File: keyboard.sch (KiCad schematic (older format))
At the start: 81 parts, among them SW10 Z, SW11 3rd, SW12 F2, SW13 E, SW14 D, SW15 X, SW16 2nd, SW17 F3, SW18 R, SW19 F, SW2 lock, SW20 C, SW21 store, SW22 F4, SW23 T, SW24 G, SW25 V, SW26 F5, SW27 Y, SW28 H, SW29 B, SW3 F1, SW30 spc, SW31 U, SW32 J, SW33 N, SW34 F6, SW35 I, SW36 K, SW37 M, SW38 equal, SW39 F7, SW4 Q, SW40 O, SW41 L, SW42 zilde, SW43 left arrow, SW44 F8, SW45 P, SW46 enter, SW47 2nd_r, SW48 menu, SW49 clear, SW5 A, SW50 ln, SW51 sin, SW52 (, SW53 7, SW54 4, SW55 1, SW56 0, SW57 esc, SW58 apps, SW59 cos, SW6 CAPS, SW60 ), SW61 8, SW62 5, SW63 2, SW64 dot, SW65 up, SW66 left, SW67 down, SW68 enter_r, SW69 tan, SW70 ,, SW71 9, SW72 6, SW73 3, SW74 negative, SW75 right, SW76 ^, SW77 ÷, SW78 ×, SW79 -, SW8 W, SW80 +, SW81 enter, SW9 S, U8 MCP23017_SS

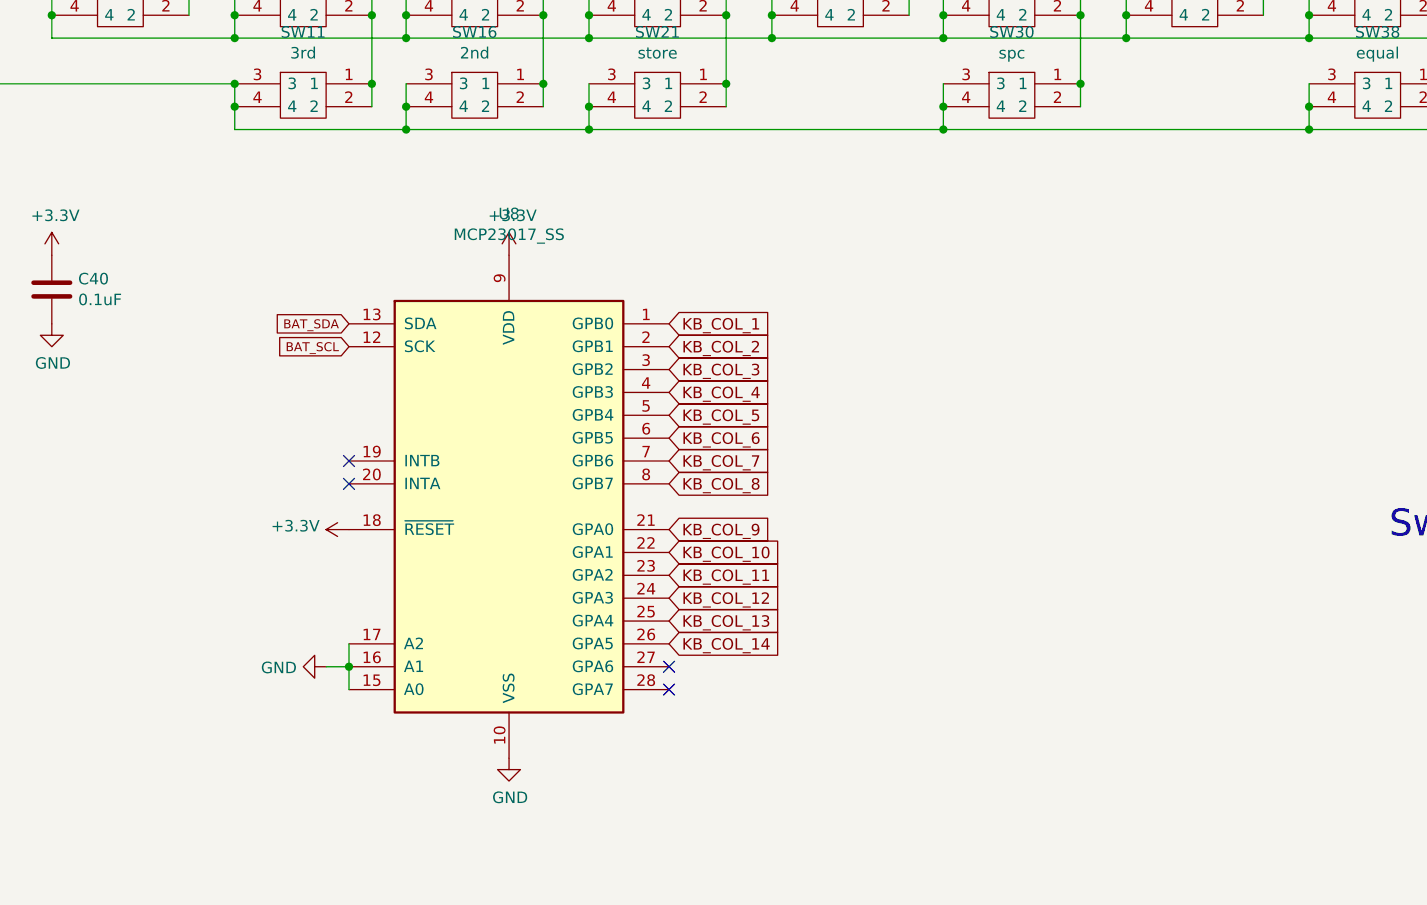
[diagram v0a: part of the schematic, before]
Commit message: Switch stuff around; Use two MCP
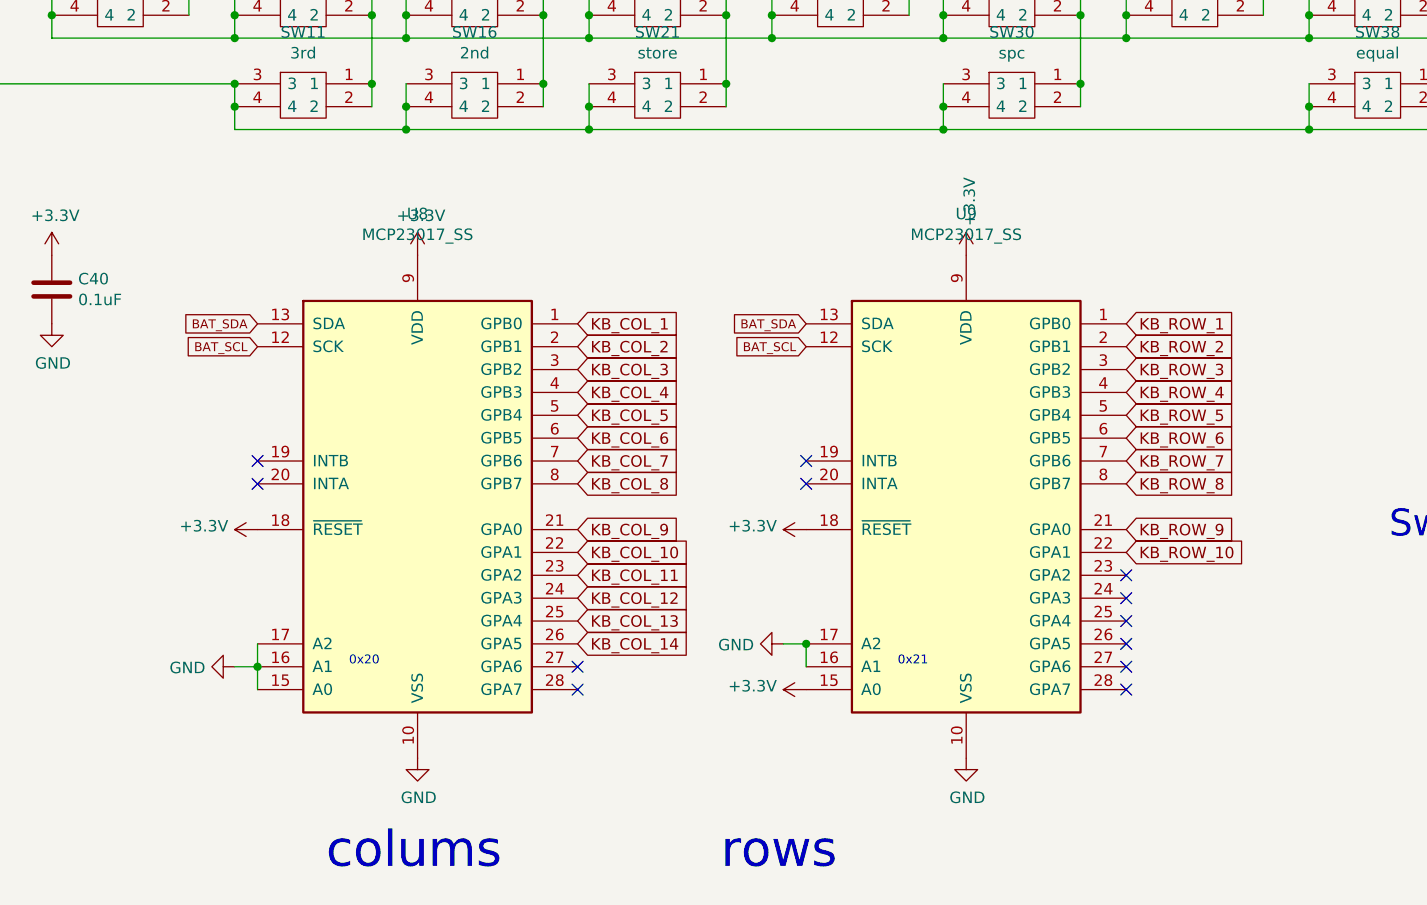
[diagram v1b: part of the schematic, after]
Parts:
- added U9: MCP23017_SS, Package_SO:SSOP-28_5.3x10.2mm_P0.65mm, symbol Interface_Expansion:MCP23017_SS
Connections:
- net +3V3: now also U9.15 (A0), U9.18 (~RESET~), U9.9 (VDD)
- net BAT_SCL: now also U9.12 (SCK)
- net BAT_SDA: now also U9.13 (SDA)
- net GND: now also U9.10 (VSS), U9.16 (A1), U9.17 (A2)
- net KB_ROW_1: now also U9.1 (GPB0)
- net KB_ROW_10: now also U9.22 (GPA1)
- net KB_ROW_2: now also U9.2 (GPB1)
- net KB_ROW_3: now also U9.3 (GPB2)
- net KB_ROW_4: now also U9.4 (GPB3)
- net KB_ROW_5: now also U9.5 (GPB4)
- net KB_ROW_6: now also U9.6 (GPB5)
- net KB_ROW_7: now also U9.7 (GPB6)
- net KB_ROW_8: now also U9.8 (GPB7)
- net KB_ROW_9: now also U9.21 (GPA0)
- no-connect marks 4 -> 12
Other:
- note added: "0x20"
- note added: "0x21"
- note added: "colums rows"
- moved on the sheet: U8
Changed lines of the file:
@@
 L Interface_Expansion:MCP23017_SS U8
 U 1 1 5F8EBE0E
-P 3200 6600
-F 0 "U8" H 3200 7881 50  0000 C CNN
-F 1 "MCP23017_SS" H 3200 7790 50  0000 C CNN
-F 2 "Package_SO:SSOP-28_5.3x10.2mm_P0.65mm" H 3400 5600 50  0001 L CNN
-F 3 "http://ww1.microchip.com/downloads/en/DeviceDoc/20001952C.pdf" H 3400 5500 50  0001 L CNN
-	1    3200 6600
-	1    0    0    -1
-$EndComp
-Text GLabel 3900 5800 2    50   Input ~ 0
+P 2800 6600
+F 0 "U8" H 2800 7881 50  0000 C CNN
+F 1 "MCP23017_SS" H 2800 7790 50  0000 C CNN
+F 2 "Package_SO:SSOP-28_5.3x10.2mm_P0.65mm" H 3000 5600 50  0001 L CNN
+F 3 "http://ww1.microchip.com/downloads/en/DeviceDoc/20001952C.pdf" H 3000 5500 50  0001 L CNN
+	1    2800 6600
+	1    0    0    -1
+$EndComp
+Text GLabel 3500 5800 2    50   Input ~ 0
 KB_COL_1
-Text GLabel 3900 5900 2    50   Input ~ 0
+Text GLabel 3500 5900 2    50   Input ~ 0
 KB_COL_2
-Text GLabel 3900 6000 2    50   Input ~ 0
+Text GLabel 3500 6000 2    50   Input ~ 0
 KB_COL_3
-Text GLabel 3900 6100 2    50   Input ~ 0
+Text GLabel 3500 6100 2    50   Input ~ 0
 KB_COL_4
-Text GLabel 3900 6200 2    50   Input ~ 0
+Text GLabel 3500 6200 2    50   Input ~ 0
 KB_COL_5
-Text GLabel 3900 6300 2    50   Input ~ 0
+Text GLabel 3500 6300 2    50   Input ~ 0
 KB_COL_6
-Text GLabel 3900 6400 2    50   Input ~ 0
+Text GLabel 3500 6400 2    50   Input ~ 0
 KB_COL_7
-Text GLabel 3900 6500 2    50   Input ~ 0
+Text GLabel 3500 6500 2    50   Input ~ 0
 KB_COL_8
-Text GLabel 3900 6700 2    50   Input ~ 0
+Text GLabel 3500 6700 2    50   Input ~ 0
 KB_COL_9
-Text GLabel 3900 6800 2    50   Input ~ 0
+Text GLabel 3500 6800 2    50   Input ~ 0
 KB_COL_10
-Text GLabel 3900 6900 2    50   Input ~ 0
+Text GLabel 3500 6900 2    50   Input ~ 0
 KB_COL_11
-Text GLabel 3900 7000 2    50   Input ~ 0
+Text GLabel 3500 7000 2    50   Input ~ 0
 KB_COL_12
-Text GLabel 3900 7100 2    50   Input ~ 0
+Text GLabel 3500 7100 2    50   Input ~ 0
 KB_COL_13
-Text GLabel 3900 7200 2    50   Input ~ 0
+Text GLabel 3500 7200 2    50   Input ~ 0
 KB_COL_14
-NoConn ~ 3900 7300
-NoConn ~ 3900 7400
-Text GLabel 2500 5800 0    39   Input ~ 0
+NoConn ~ 3500 7300
+NoConn ~ 3500 7400
+Text GLabel 2100 5800 0    39   Input ~ 0
 BAT_SDA
-Text GLabel 2500 5900 0    39   Input ~ 0
+Text GLabel 2100 5900 0    39   Input ~ 0
 BAT_SCL
 $Comp
 L power:GND #PWR0130
 U 1 1 5F97902E
-P 3200 7700
-F 0 "#PWR0130" H 3200 7450 50  0001 C CNN
-F 1 "GND" H 3205 7527 50  0000 C CNN
-F 2 "" H 3200 7700 50  0001 C CNN
-F 3 "" H 3200 7700 50  0001 C CNN
-	1    3200 7700
+P 2800 7700
+F 0 "#PWR0130" H 2800 7450 50  0001 C CNN
+F 1 "GND" H 2805 7527 50  0000 C CNN
+F 2 "" H 2800 7700 50  0001 C CNN
+F 3 "" H 2800 7700 50  0001 C CNN
+	1    2800 7700
 	1    0    0    -1
 $EndComp
@@
 L power:+3.3V #PWR0131
 U 1 1 5F9B509C
-P 3200 5500
-F 0 "#PWR0131" H 3200 5350 50  0001 C CNN
-F 1 "+3.3V" H 3215 5673 50  0000 C CNN
-F 2 "" H 3200 5500 50  0001 C CNN
-F 3 "" H 3200 5500 50  0001 C CNN
-	1    3200 5500
+P 2800 5500
+F 0 "#PWR0131" H 2800 5350 50  0001 C CNN
+F 1 "+3.3V" H 2815 5673 50  0000 C CNN
+F 2 "" H 2800 5500 50  0001 C CNN
+F 3 "" H 2800 5500 50  0001 C CNN
+	1    2800 5500
 	1    0    0    -1
 $EndComp
@@
 	1    0    0    -1
 $EndComp
-NoConn ~ 2500 6400
-NoConn ~ 2500 6500
+NoConn ~ 2100 6400
+NoConn ~ 2100 6500
 $Comp
 L power:+3.3V #PWR0134
 U 1 1 5F9F0EAC
-P 2500 6700
-F 0 "#PWR0134" H 2500 6550 50  0001 C CNN
-F 1 "+3.3V" V 2515 6828 50  0000 L CNN
-F 2 "" H 2500 6700 50  0001 C CNN
-F 3 "" H 2500 6700 50  0001 C CNN
-	1    2500 6700
+P 2100 6700
+F 0 "#PWR0134" H 2100 6550 50  0001 C CNN
+F 1 "+3.3V" V 2115 6828 50  0000 L CNN
+F 2 "" H 2100 6700 50  0001 C CNN
+F 3 "" H 2100 6700 50  0001 C CNN
+	1    2100 6700
 	0    -1   -1   0
 $EndComp
@@
 L power:GND #PWR0135
 U 1 1 5F9F243C
-P 2400 7300
-F 0 "#PWR0135" H 2400 7050 50  0001 C CNN
-F 1 "GND" V 2405 7172 50  0000 R CNN
-F 2 "" H 2400 7300 50  0001 C CNN
-F 3 "" H 2400 7300 50  0001 C CNN
-	1    2400 7300
+P 2000 7300
+F 0 "#PWR0135" H 2000 7050 50  0001 C CNN
+F 1 "GND" V 2005 7172 50  0000 R CNN
+F 2 "" H 2000 7300 50  0001 C CNN
+F 3 "" H 2000 7300 50  0001 C CNN
+	1    2000 7300
 	0    1    1    0
 $EndComp
 Wire Wire Line
-	2400 7300 2500 7300
-Wire Wire Line
-	2500 7200 2500 7300
-Connection ~ 2500 7300
-Wire Wire Line
-	2500 7300 2500 7400
+	2000 7300 2100 7300
+Wire Wire Line
+	2100 7200 2100 7300
+Connection ~ 2100 7300
+Wire Wire Line
+	2100 7300 2100 7400
 Text Notes 7050 6750 0    118  ~ 0
 Switches: FSM4JSMAATR
@@
 Wire Wire Line
 	10750 1650 10750 1750
+$Comp
+L Interface_Expansion:MCP23017_SS U9
+U 1 1 614CD4FF
+P 5200 6600
+F 0 "U9" H 5200 7881 50  0000 C CNN
+F 1 "MCP23017_SS" H 5200 7790 50  0000 C CNN
+F 2 "Package_SO:SSOP-28_5.3x10.2mm_P0.65mm" H 5400 5600 50  0001 L CNN
+F 3 "http://ww1.microchip.com/downloads/en/DeviceDoc/20001952C.pdf" H 5400 5500 50  0001 L CNN
+	1    5200 6600
+	1    0    0    -1
+$EndComp
+Text GLabel 4500 5800 0    39   Input ~ 0
+BAT_SDA
+Text GLabel 4500 5900 0    39   Input ~ 0
+BAT_SCL
+NoConn ~ 4500 6400
+NoConn ~ 4500 6500
+$Comp
+L power:+3.3V #PWR0125
+U 1 1 61601386
+P 4500 6700
+F 0 "#PWR0125" H 4500 6550 50  0001 C CNN
+F 1 "+3.3V" V 4515 6828 50  0000 L CNN
+F 2 "" H 4500 6700 50  0001 C CNN
+F 3 "" H 4500 6700 50  0001 C CNN
+	1    4500 6700
+	0    -1   -1   0
+$EndComp
+$Comp
+L power:GND #PWR0136
+U 1 1 61602403
+P 4400 7200
+F 0 "#PWR0136" H 4400 6950 50  0001 C CNN
+F 1 "GND" V 4405 7072 50  0000 R CNN
+F 2 "" H 4400 7200 50  0001 C CNN
+F 3 "" H 4400 7200 50  0001 C CNN
+	1    4400 7200
+	0    1    1    0
+$EndComp
+Wire Wire Line
+	4400 7200 4500 7200
+Wire Wire Line
+	4500 7300 4500 7200
+Connection ~ 4500 7200
+$Comp
+L power:+3.3V #PWR0137
+U 1 1 6166826B
+P 4500 7400
+F 0 "#PWR0137" H 4500 7250 50  0001 C CNN
+F 1 "+3.3V" V 4515 7528 50  0000 L CNN
+F 2 "" H 4500 7400 50  0001 C CNN
+F 3 "" H 4500 7400 50  0001 C CNN
+	1    4500 7400
+	0    -1   -1   0
+$EndComp
+$Comp
+L power:GND #PWR0138
+U 1 1 6166895E
+P 5200 7700
+F 0 "#PWR0138" H 5200 7450 50  0001 C CNN
+F 1 "GND" H 5205 7527 50  0000 C CNN
+F 2 "" H 5200 7700 50  0001 C CNN
+F 3 "" H 5200 7700 50  0001 C CNN
+	1    5200 7700
+	1    0    0    -1
+$EndComp
+Text GLabel 5900 5800 2    50   Input ~ 0
+KB_ROW_1
+Text GLabel 5900 5900 2    50   Input ~ 0
+KB_ROW_2
+Text GLabel 5900 6000 2    50   Input ~ 0
+KB_ROW_3
+Text GLabel 5900 6100 2    50   Input ~ 0
+KB_ROW_4
+Text GLabel 5900 6200 2    50   Input ~ 0
+KB_ROW_5
+Text GLabel 5900 6300 2    50   Input ~ 0
+KB_ROW_6
+Text GLabel 5900 6400 2    50   Input ~ 0
+KB_ROW_7
+Text GLabel 5900 6500 2    50   Input ~ 0
+KB_ROW_8
+Text GLabel 5900 6700 2    50   Input ~ 0
+KB_ROW_9
+Text GLabel 5900 6800 2    50   Input ~ 0
+KB_ROW_10
+$Comp
+L power:+3.3V #PWR0140
+U 1 1 61669430
+P 5200 5500
+F 0 "#PWR0140" H 5200 5350 50  0001 C CNN
+F 1 "+3.3V" V 5215 5628 50  0000 L CNN
+F 2 "" H 5200 5500 50  0001 C CNN
+F 3 "" H 5200 5500 50  0001 C CNN
+	1    5200 5500
+	1    0    0    -1
+$EndComp
+NoConn ~ 5900 6900
+NoConn ~ 5900 7000
+NoConn ~ 5900 7100
+NoConn ~ 5900 7200
+NoConn ~ 5900 7300
+NoConn ~ 5900 7400
+Text Notes 2400 8200 0    157  ~ 0
+colums              rows
+Text Notes 2500 7300 0    39   ~ 0
+0x20
+Text Notes 4900 7300 0    39   ~ 0
+0x21
 $EndSCHEMATC

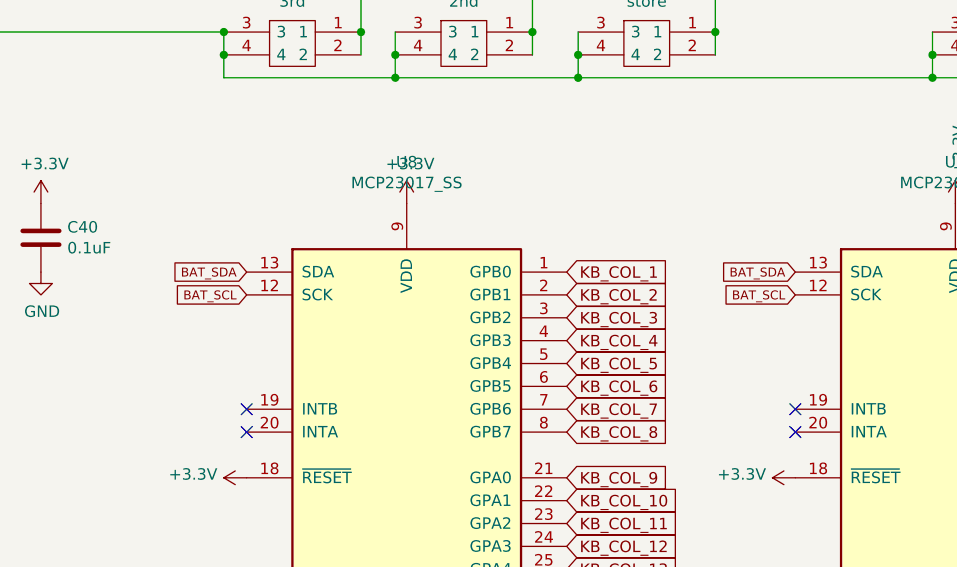
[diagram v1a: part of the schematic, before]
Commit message: Move touchscreen to user i2c with jumpers
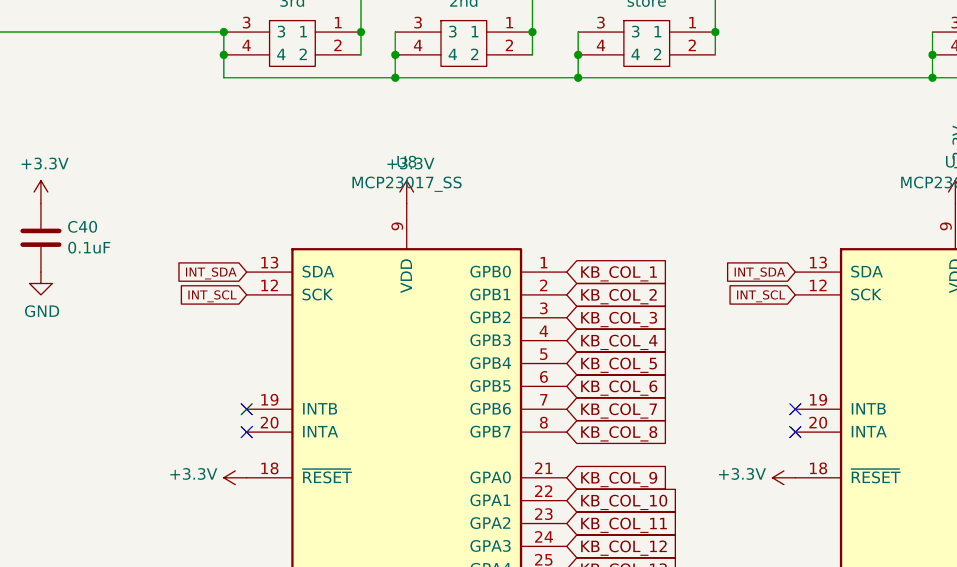
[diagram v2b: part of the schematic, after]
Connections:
- net BAT_SCL renamed INT_SCL
- net BAT_SDA renamed INT_SDA
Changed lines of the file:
@@
 NoConn ~ 3500 7400
 Text GLabel 2100 5800 0    39   Input ~ 0
-BAT_SDA
+INT_SDA
 Text GLabel 2100 5900 0    39   Input ~ 0
-BAT_SCL
+INT_SCL
 $Comp
 L power:GND #PWR0130
@@
 $EndComp
 Text GLabel 4500 5800 0    39   Input ~ 0
-BAT_SDA
+INT_SDA
 Text GLabel 4500 5900 0    39   Input ~ 0
-BAT_SCL
+INT_SCL
 NoConn ~ 4500 6400
 NoConn ~ 4500 6500
